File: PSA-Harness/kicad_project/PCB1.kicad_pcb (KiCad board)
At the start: 4 copper layers, 22.4 x 46.8 mm, 5 parts, among them J10 B2B_1, J11 B2B_2, J4 to_car_1, J5 to_car_2, J6 to_car_3

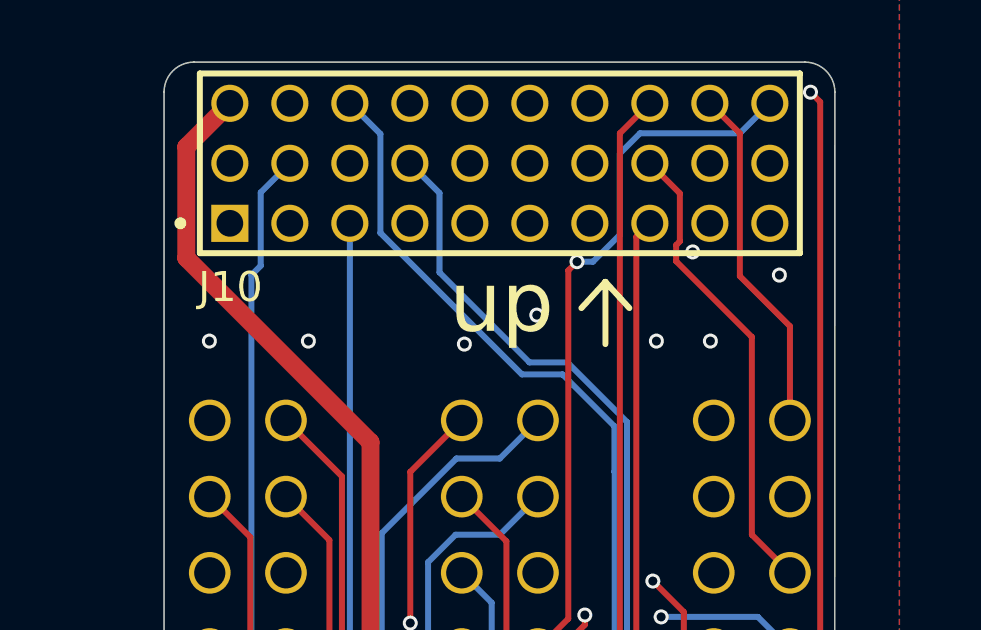
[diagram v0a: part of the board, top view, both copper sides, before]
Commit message: move all psa harness components to top layer
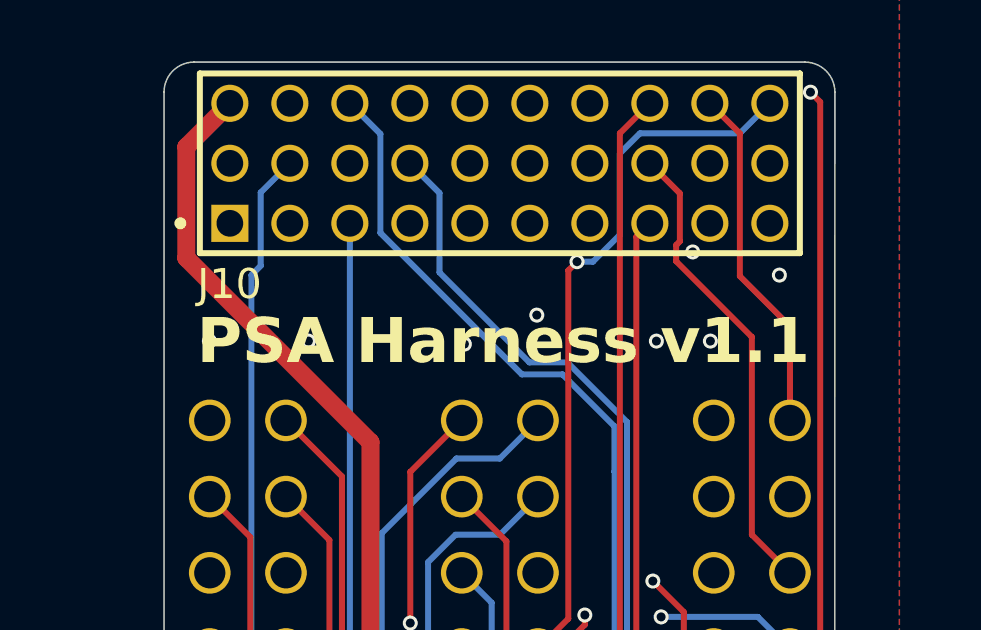
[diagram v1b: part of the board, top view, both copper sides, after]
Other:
- board text added: "PSA Harness v1.1"
- board text removed: "up"
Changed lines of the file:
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@@
 		(at 126.682 104.174)
 		(property "Reference" "J10"
-			(at 0.018 2.126 0)
+			(at -0.012 2.026 0)
 			(layer "F.SilkS")
 			(effects
@@
 		)
 	)
-	(gr_line
-		(start 140 107)
-		(end 139.2 106.125)
-		(stroke
-			(width 0.2)
-			(type solid)
-		)
-		(layer "F.SilkS")
-	)
-	(gr_line
-		(start 139.2 108.2)
-		(end 139.2 106.125)
-		(stroke
-			(width 0.2)
-			(type solid)
-		)
-		(layer "F.SilkS")
-	)
-	(gr_line
-		(start 139.2 106.125)
-		(end 138.4 107)
-		(stroke
-			(width 0.2)
-			(type solid)
-		)
-		(layer "F.SilkS")
-	)
 	(gr_arc
 		(start 146.84 144.55)
@@
 		(layer "Edge.Cuts")
 	)
-	(gr_text "up"
-		(at 134 108 0)
+	(gr_text "PSA Harness v1.1"
+		(at 125.58 108.98 0)
 		(layer "F.SilkS")
 		(effects
 			(font
-				(size 2 2)
-				(thickness 0.25)
+				(size 1.5 1.5)
+				(thickness 0.3)
+				(bold yes)
 			)
 			(justify left bottom)

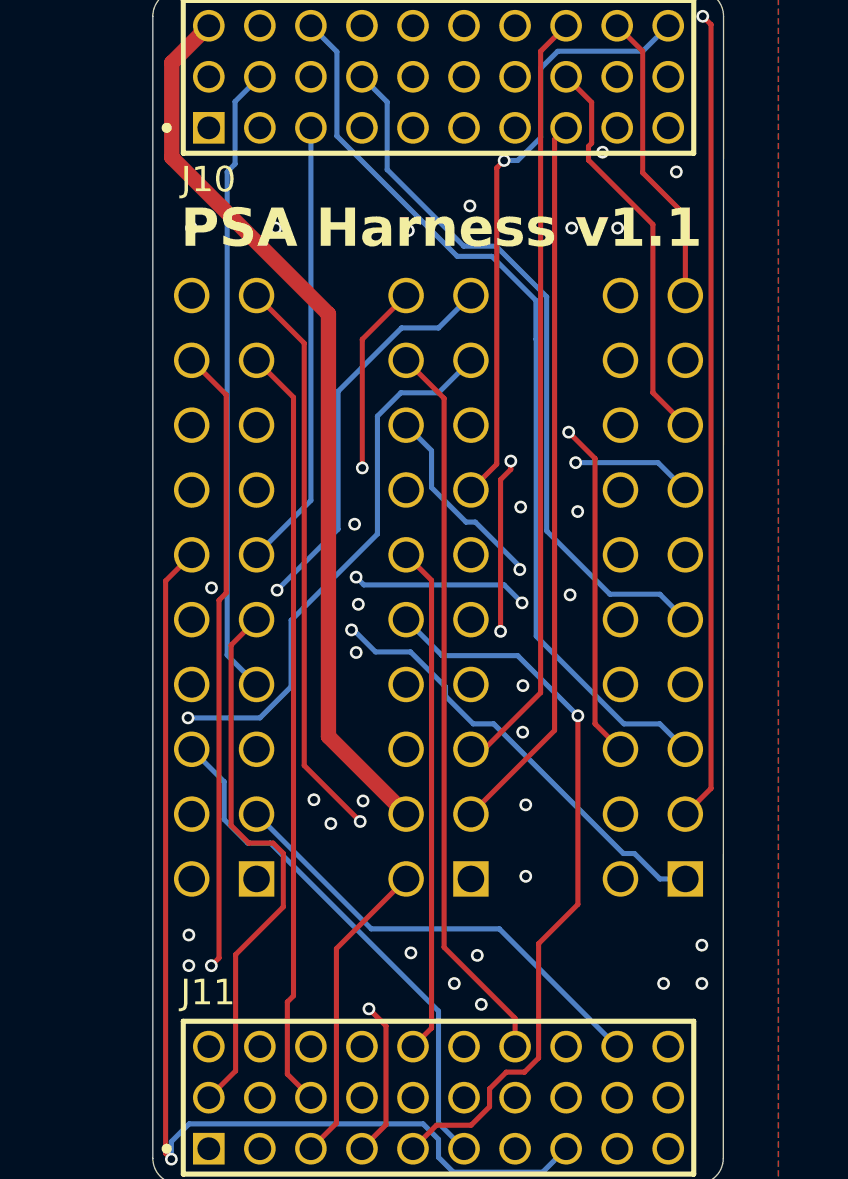
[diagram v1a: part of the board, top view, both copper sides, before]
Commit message: CAN signals routed
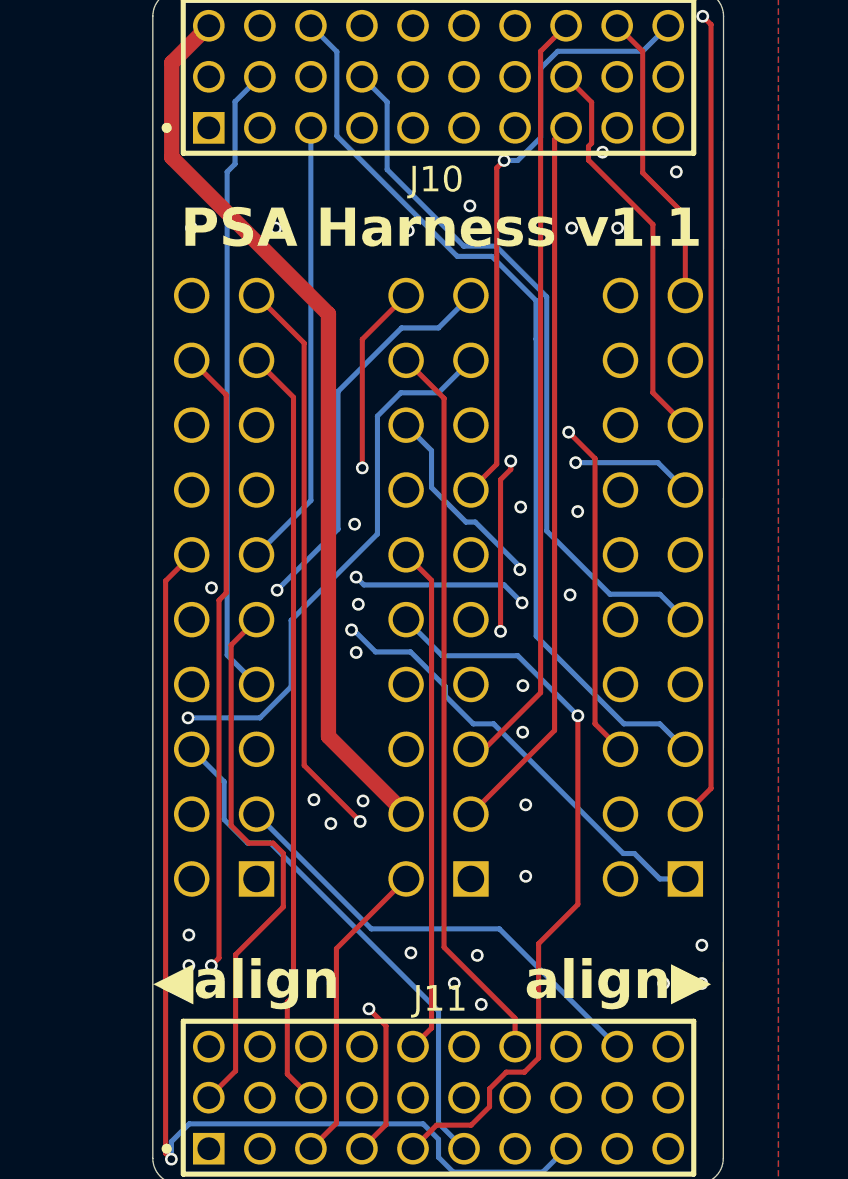
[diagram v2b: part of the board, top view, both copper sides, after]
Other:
- board text added: "align▶"
- board text added: "◀align"
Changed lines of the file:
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@@
 		(at 126.682 104.174)
 		(property "Reference" "J10"
-			(at -0.012 2.026 0)
+			(at 8.918 2.026 0)
 			(layer "F.SilkS")
 			(effects
@@
 		)
 		(property "Value" "B2B_1"
-			(at 11.97 2.86 0)
+			(at 1.318 -6.274 0)
 			(layer "F.Fab")
 			(effects
@@
 		(at 126.682 144.174)
 		(property "Reference" "J11"
-			(at -0.032 -6.124 0)
+			(at 9.068 -5.874 0)
 			(layer "F.SilkS")
 			(effects
@@
 		)
 		(property "Value" "B2B_2"
-			(at 11.97 2.86 0)
+			(at 1.068 2.626 0)
 			(layer "F.Fab")
 			(effects
@@
 		(layer "Edge.Cuts")
 	)
+	(gr_text "◀align"
+		(at 124.5 138.45 0)
+		(layer "F.SilkS")
+		(effects
+			(font
+				(size 1.5 1.5)
+				(thickness 0.3)
+				(bold yes)
+			)
+			(justify left bottom)
+		)
+	)
+	(gr_text "align▶"
+		(at 139.05 138.45 0)
+		(layer "F.SilkS")
+		(effects
+			(font
+				(size 1.5 1.5)
+				(thickness 0.3)
+				(bold yes)
+			)
+			(justify left bottom)
+		)
+	)
 	(gr_text "PSA Harness v1.1"
